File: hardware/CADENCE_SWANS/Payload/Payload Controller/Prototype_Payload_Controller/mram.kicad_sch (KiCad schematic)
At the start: 3 parts

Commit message: updates
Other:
- moved on the sheet: U4C, U4D, U4E
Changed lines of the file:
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@@
 	)
 	(no_connect
-		(at 69.85 163.83)
+		(at 238.76 143.51)
 	)
 	(no_connect
-		(at 88.9 163.83)
+		(at 257.81 143.51)
 	)
 	(no_connect
-		(at 69.85 156.21)
+		(at 238.76 135.89)
 	)
 	(no_connect
-		(at 69.85 158.75)
+		(at 238.76 138.43)
 	)
 	(no_connect
-		(at 88.9 156.21)
+		(at 257.81 135.89)
 	)
 	(no_connect
-		(at 69.85 161.29)
+		(at 238.76 140.97)
 	)
 	(no_connect
-		(at 88.9 161.29)
+		(at 257.81 140.97)
 	)
 	(no_connect
-		(at 88.9 158.75)
+		(at 257.81 138.43)
 	)
 	(bus_entry
@@
 	(wire
 		(pts
-			(xy 173.99 135.89) (xy 179.07 135.89)
+			(xy 167.64 124.46) (xy 172.72 124.46)
 		)
 		(stroke
@@
 	(wire
 		(pts
-			(xy 68.58 138.43) (xy 73.66 138.43)
+			(xy 82.55 146.05) (xy 87.63 146.05)
 		)
 		(stroke
@@
 	(wire
 		(pts
-			(xy 68.58 140.97) (xy 73.66 140.97)
+			(xy 82.55 148.59) (xy 87.63 148.59)
 		)
 		(stroke
@@
 	(wire
 		(pts
-			(xy 68.58 143.51) (xy 73.66 143.51)
+			(xy 82.55 151.13) (xy 87.63 151.13)
 		)
 		(stroke
@@
 	(wire
 		(pts
-			(xy 149.86 138.43) (xy 154.94 138.43)
+			(xy 143.51 127) (xy 148.59 127)
 		)
 		(stroke
@@
 	(wire
 		(pts
-			(xy 149.86 135.89) (xy 154.94 135.89)
+			(xy 143.51 124.46) (xy 148.59 124.46)
 		)
 		(stroke
@@
 	(wire
 		(pts
-			(xy 173.99 140.97) (xy 179.07 140.97)
+			(xy 167.64 129.54) (xy 172.72 129.54)
 		)
 		(stroke
@@
 	(wire
 		(pts
-			(xy 173.99 133.35) (xy 179.07 133.35)
+			(xy 167.64 121.92) (xy 172.72 121.92)
 		)
 		(stroke
@@
 	(wire
 		(pts
-			(xy 173.99 138.43) (xy 179.07 138.43)
+			(xy 167.64 127) (xy 172.72 127)
 		)
 		(stroke
@@
 	(wire
 		(pts
-			(xy 149.86 133.35) (xy 154.94 133.35)
+			(xy 143.51 121.92) (xy 148.59 121.92)
 		)
 		(stroke
@@
 	(wire
 		(pts
-			(xy 149.86 140.97) (xy 154.94 140.97)
+			(xy 143.51 129.54) (xy 148.59 129.54)
 		)
 		(stroke
@@
 	)
 	(label "D0"
-		(at 149.86 133.35 0)
+		(at 143.51 121.92 0)
 		(effects
 			(font
@@
 	)
 	(label "D5"
-		(at 179.07 138.43 180)
+		(at 172.72 127 180)
 		(effects
 			(font
@@
 	)
 	(label "OE"
-		(at 68.58 140.97 0)
+		(at 82.55 148.59 0)
 		(effects
 			(font
@@
 	)
 	(label "D6"
-		(at 179.07 135.89 180)
+		(at 172.72 124.46 180)
 		(effects
 			(font
@@
 	)
 	(label "D7"
-		(at 179.07 133.35 180)
+		(at 172.72 121.92 180)
 		(effects
 			(font
@@
 	)
 	(label "WE"
-		(at 68.58 143.51 0)
+		(at 82.55 151.13 0)
 		(effects
 			(font
@@
 	)
 	(label "D3"
-		(at 149.86 140.97 0)
+		(at 143.51 129.54 0)
 		(effects
 			(font
@@
 	)
 	(label "D1"
-		(at 149.86 135.89 0)
+		(at 143.51 124.46 0)
 		(effects
 			(font
@@
 	)
 	(label "D2"
-		(at 149.86 138.43 0)
+		(at 143.51 127 0)
 		(effects
 			(font
@@
 	)
 	(label "D4"
-		(at 179.07 140.97 180)
+		(at 172.72 129.54 180)
 		(effects
 			(font
@@
 	)
 	(label "CS"
-		(at 68.58 138.43 0)
+		(at 82.55 146.05 0)
 		(effects
 			(font
@@
 	(symbol
 		(lib_id "Payload_Controller_EM:MR4A08B")
-		(at 76.2 146.05 0)
+		(at 90.17 153.67 0)
 		(unit 4)
 		(exclude_from_sim no)
@@
 		(fields_autoplaced yes)
 		(property "Reference" "U4"
-			(at 90.17 140.3349 0)
+			(at 104.14 147.9549 0)
 			(effects
 				(font
@@
 		)
 		(property "Value" "~"
-			(at 90.17 142.24 0)
+			(at 104.14 149.86 0)
 			(effects
 				(font
@@
 		)
 		(property "Footprint" ""
-			(at 76.2 146.05 0)
+			(at 90.17 153.67 0)
 			(effects
 				(font
@@
 		)
 		(property "Datasheet" ""
-			(at 76.2 146.05 0)
+			(at 90.17 153.67 0)
 			(effects
 				(font
@@
 		)
 		(property "Description" ""
-			(at 76.2 146.05 0)
+			(at 90.17 153.67 0)
 			(effects
 				(font
@@
 	(symbol
 		(lib_id "Payload_Controller_EM:MR4A08B")
-		(at 157.48 143.51 0)
+		(at 151.13 132.08 0)
 		(unit 3)
 		(exclude_from_sim no)
@@
 		(fields_autoplaced yes)
 		(property "Reference" "U4"
-			(at 164.465 127 0)
+			(at 158.115 115.57 0)
 			(effects
 				(font
@@
 		)
 		(property "Value" "~"
-			(at 164.465 129.54 0)
+			(at 158.115 118.11 0)
 			(effects
 				(font
@@
 		)
 		(property "Footprint" ""
-			(at 157.48 143.51 0)
+			(at 151.13 132.08 0)
 			(effects
 				(font
@@
 		)
 		(property "Datasheet" ""
-			(at 157.48 143.51 0)
+			(at 151.13 132.08 0)
 			(effects
 				(font
@@
 		)
 		(property "Description" ""
-			(at 157.48 143.51 0)
+			(at 151.13 132.08 0)
 			(effects
 				(font
@@
 	(symbol
 		(lib_id "Payload_Controller_EM:MR4A08B")
-		(at 72.39 166.37 0)
+		(at 241.3 146.05 0)
 		(unit 5)
 		(exclude_from_sim no)
@@
 		(fields_autoplaced yes)
 		(property "Reference" "U4"
-			(at 79.375 149.86 0)
+			(at 248.285 129.54 0)
 			(effects
 				(font
@@
 		)
 		(property "Value" "~"
-			(at 79.375 152.4 0)
+			(at 248.285 132.08 0)
 			(effects
 				(font
@@
 		)
 		(property "Footprint" ""
-			(at 72.39 166.37 0)
+			(at 241.3 146.05 0)
 			(effects
 				(font
@@
 		)
 		(property "Datasheet" ""
-			(at 72.39 166.37 0)
+			(at 241.3 146.05 0)
 			(effects
 				(font
@@
 		)
 		(property "Description" ""
-			(at 72.39 166.37 0)
+			(at 241.3 146.05 0)
 			(effects
 				(font

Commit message: updated MRAM Schematic Symbol
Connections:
- net D0 renamed MRAM_DATA0
- net D1 renamed MRAM_DATA1
- net D2 renamed MRAM_DATA2
- net D3 renamed MRAM_DATA3
- net D4 renamed MRAM_DATA4
- net D5 renamed MRAM_DATA5
- net D6 renamed MRAM_DATA6
- net D7 renamed MRAM_DATA7
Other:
- moved on the sheet: U4B, U4D

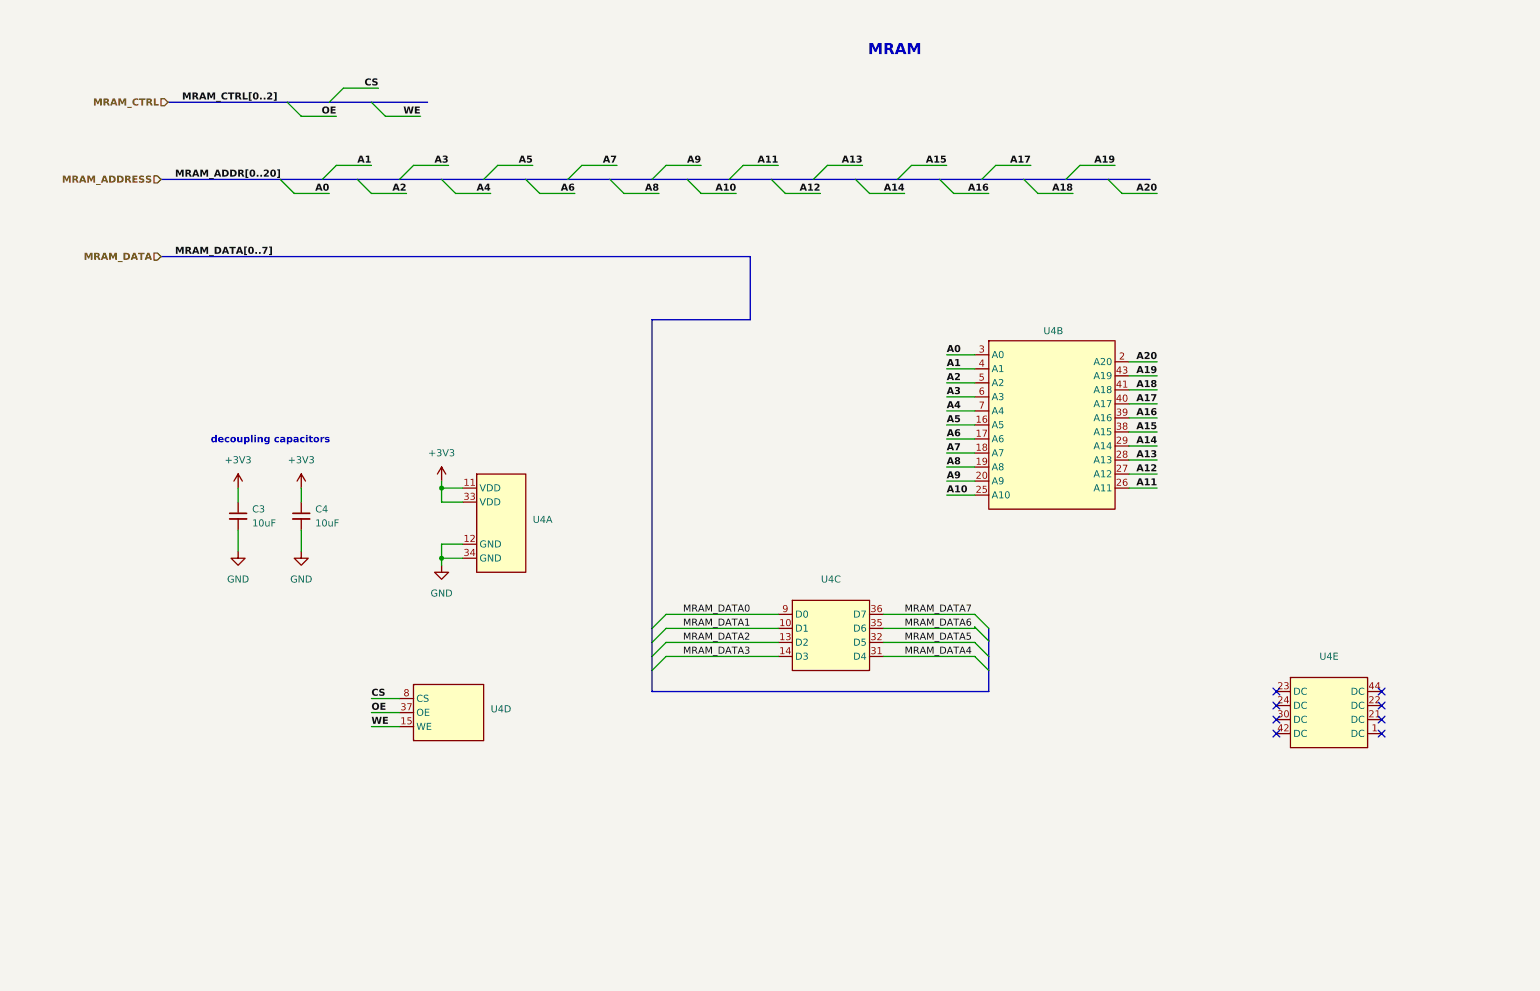
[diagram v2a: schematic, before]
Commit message: resolved bus naming issues
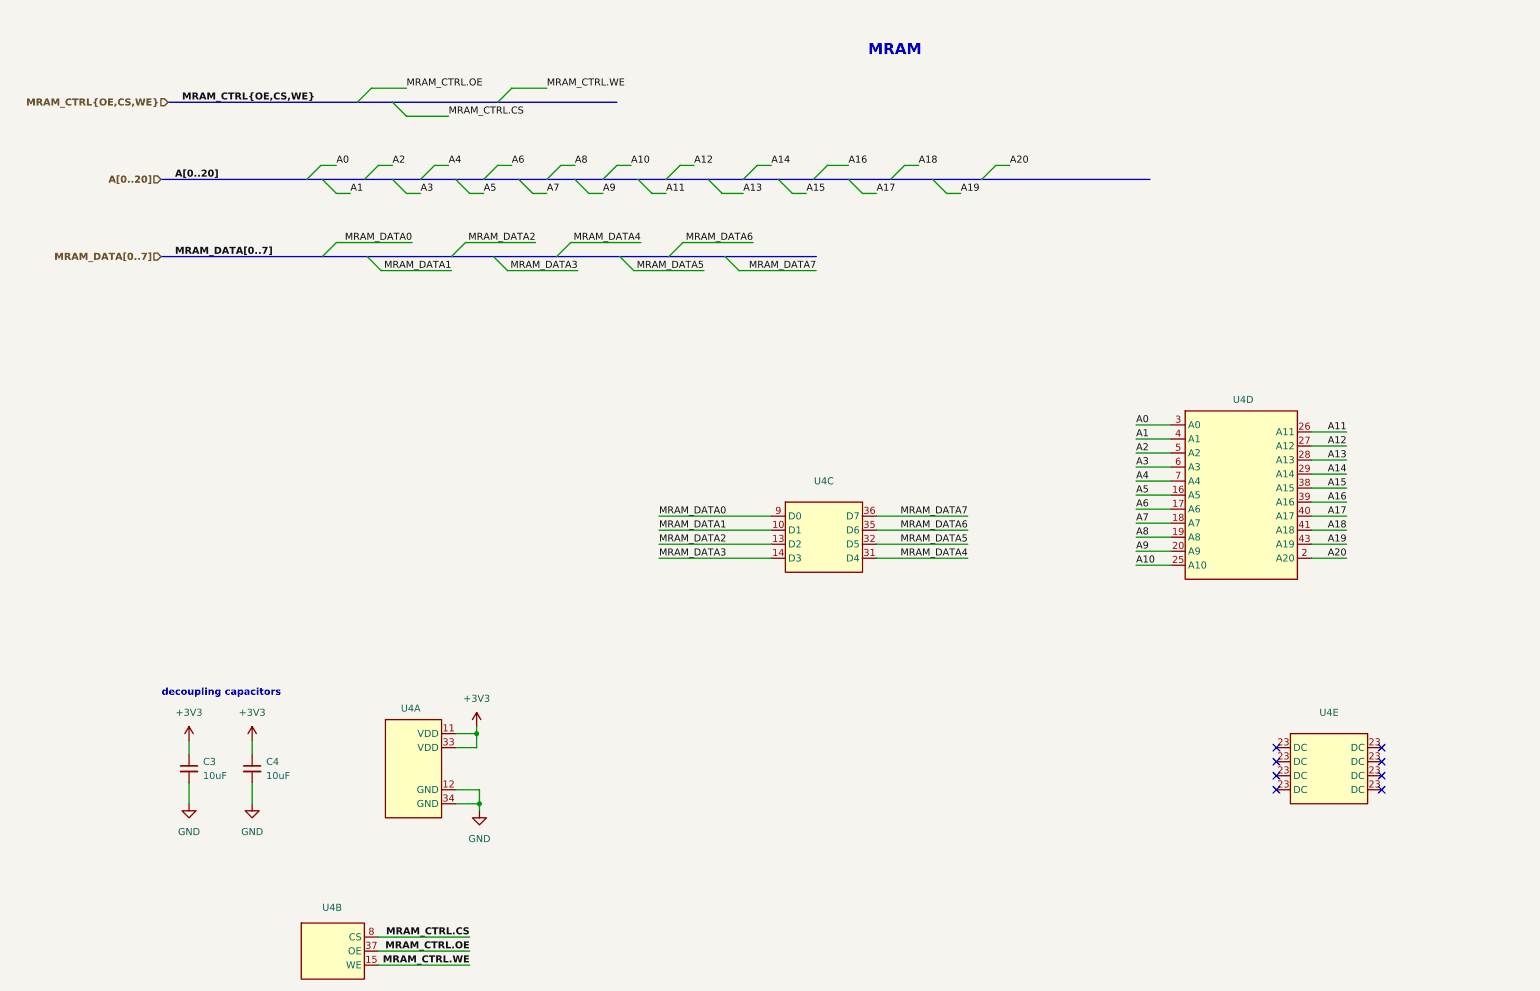
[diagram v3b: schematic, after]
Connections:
- net A0: now also U4.3 (A0); no longer U4.3 (A0)
- net A1: now also U4.4 (A1); no longer U4.4 (A1)
- net A10: now also U4.25 (A10); no longer U4.25 (A10)
- net A11: now also U4.26 (A11); no longer U4.26 (A11)
- net A12: now also U4.27 (A12); no longer U4.27 (A12)
- net A13: now also U4.28 (A13); no longer U4.28 (A13)
- net A14: now also U4.29 (A14); no longer U4.29 (A14)
- net A15: now also U4.38 (A15); no longer U4.38 (A15)
- net A16: now also U4.39 (A16); no longer U4.39 (A16)
- net A17: now also U4.40 (A17); no longer U4.40 (A17)
- net A18: now also U4.41 (A18); no longer U4.41 (A18)
- net A19: now also U4.43 (A19); no longer U4.43 (A19)
- net A2: now also U4.5 (A2); no longer U4.5 (A2)
- net A20: now also U4.2 (A20); no longer U4.2 (A20)
- net A3: now also U4.6 (A3); no longer U4.6 (A3)
- net A4: now also U4.7 (A4); no longer U4.7 (A4)
- net A5: now also U4.16 (A5); no longer U4.16 (A5)
- net A6: now also U4.17 (A6); no longer U4.17 (A6)
- net A7: now also U4.18 (A7); no longer U4.18 (A7)
- net A8: now also U4.19 (A8); no longer U4.19 (A8)
- net A9: now also U4.20 (A9); no longer U4.20 (A9)
- removed net CS: U4.8 (CS)
- removed net OE: U4.37 (OE)
- removed net WE: U4.15 (WE)
- new net MRAM_CTRL.CS: U4.8 (CS)
- new net MRAM_CTRL.OE: U4.37 (OE)
- new net MRAM_CTRL.WE: U4.15 (WE)
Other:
- moved on the sheet: C3, C4, U4A, U4C, U4E

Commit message: updated power regulators
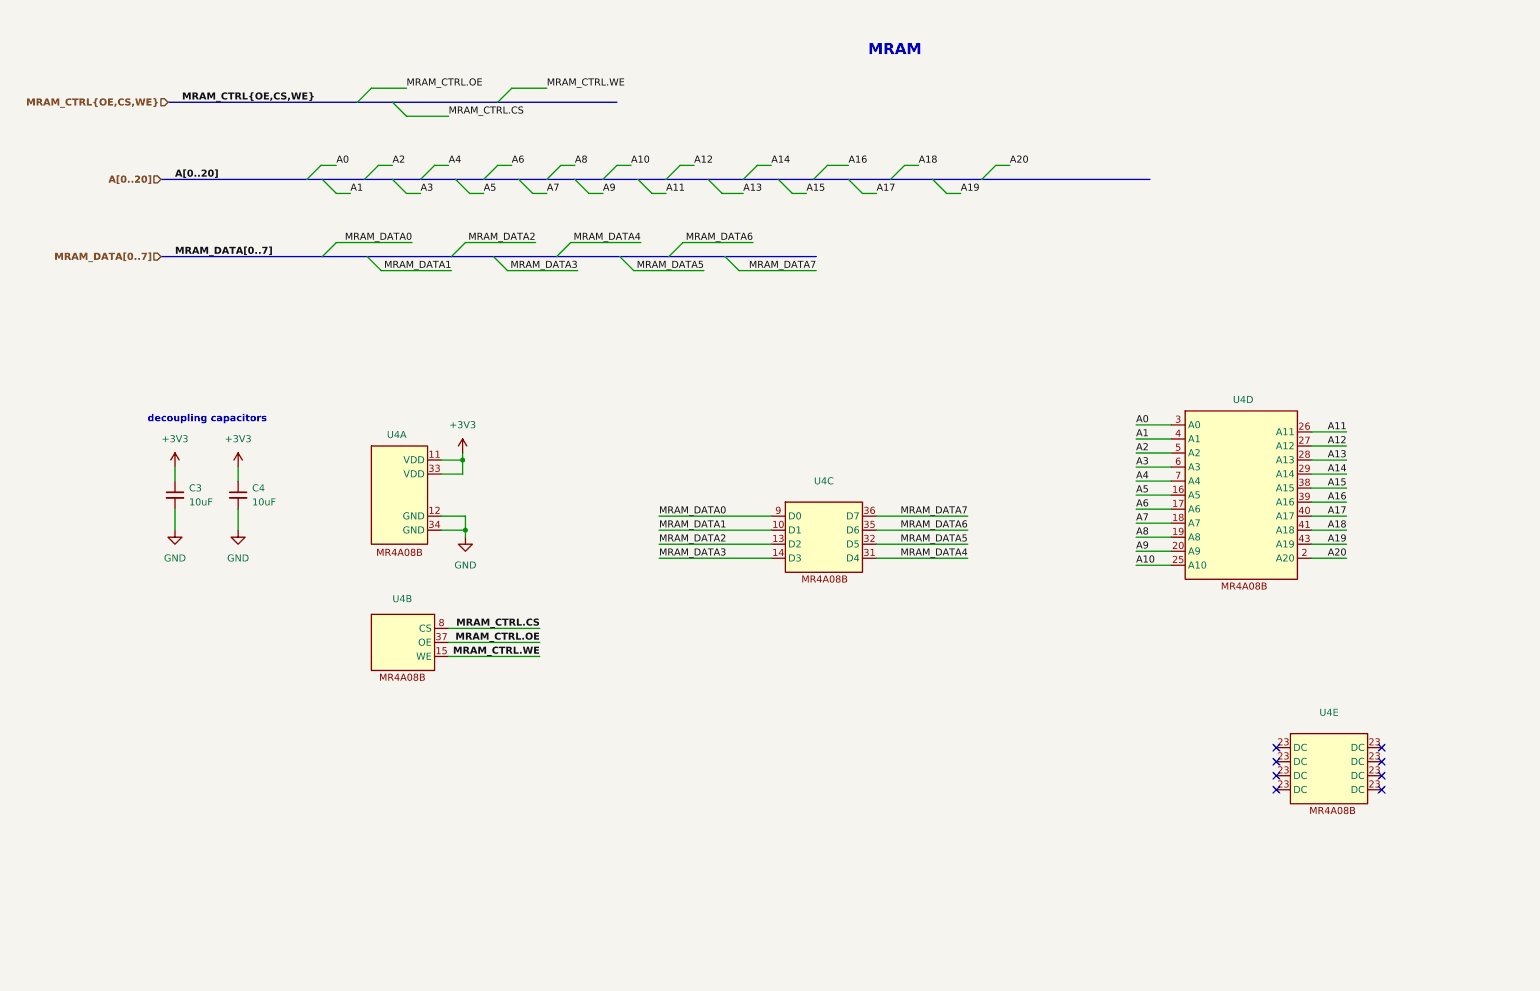
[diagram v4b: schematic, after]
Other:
- moved on the sheet: C3, C4

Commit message: cleaned up schematics and assigned footprints for resistors and capacitors
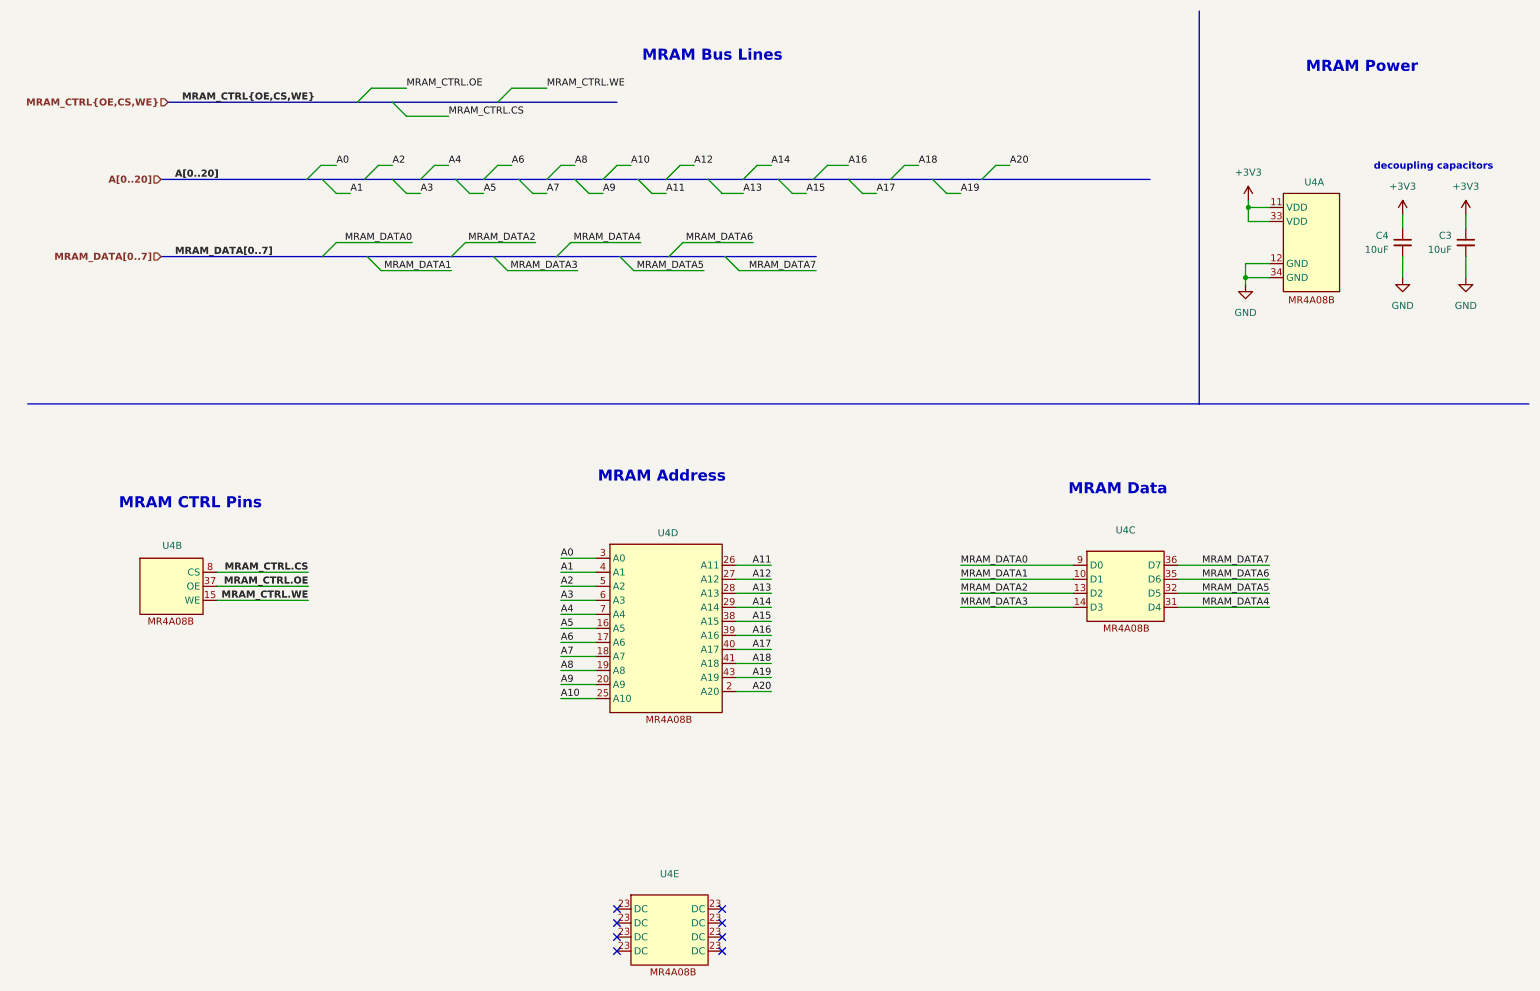
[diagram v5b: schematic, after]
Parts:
- C3, C4: footprint (none) -> Capacitor_SMD:C_0603_1608Metric
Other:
- note added: "MRAM Address"
- note added: "MRAM Bus Lines"
- note added: "MRAM CTRL Pins"
- note added: "MRAM Data"
- note added: "MRAM Power"
- note removed: "MRAM"
- moved on the sheet: C3, C4, U4A, U4B, U4C, U4D, U4E

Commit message: assigned more footprints
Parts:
- U4: footprint (none) -> Package_SO:TSOP-II-44_10.16x18.41mm_P0.8mm
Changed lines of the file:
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@@
 			)
 		)
-		(property "Footprint" ""
+		(property "Footprint" "Package_SO:TSOP-II-44_10.16x18.41mm_P0.8mm"
 			(at 33.02 121.92 0)
 			(effects
@@
 			)
 		)
-		(property "Footprint" ""
+		(property "Footprint" "Package_SO:TSOP-II-44_10.16x18.41mm_P0.8mm"
 			(at 118.11 139.7 0)
 			(effects
@@
 			)
 		)
-		(property "Footprint" ""
+		(property "Footprint" "Package_SO:TSOP-II-44_10.16x18.41mm_P0.8mm"
 			(at 250.19 63.5 0)
 			(effects
@@
 			)
 		)
-		(property "Footprint" ""
+		(property "Footprint" "Package_SO:TSOP-II-44_10.16x18.41mm_P0.8mm"
 			(at 204.47 123.19 0)
 			(effects
@@
 			)
 		)
-		(property "Footprint" ""
+		(property "Footprint" "Package_SO:TSOP-II-44_10.16x18.41mm_P0.8mm"
 			(at 121.92 185.42 0)
 			(effects
